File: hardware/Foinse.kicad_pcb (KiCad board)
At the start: 4 copper layers, 60 x 60 mm, 150 parts, among them J1 Conn_02x03_Odd_Even, J10 Conn_02x03_Odd_Even, J2 2060-1452, J3 ESQ-110-14-G-D, J4 PJ-002AH, J5 2060-1452/998-404, J8 2601-1108, J9 USB_C_Receptacle_USB2.0_16P, Q1 AO3400A, Q10 AO3400A, Q11 AO3400A, Q12 AO3400A, Q13 AO3400A, Q14 AO3400A, Q2 AO3400A, Q3 AO3400A, Q4 AO3400A, Q5 AO3400A, Q6 AO3400A, Q7 AO3400A, Q8 AO3400A, Q9 AO3400A, U1 STM32F072C8Tx, U10 LTV-817, U11 LTV-817, U12 LTV-817, U13 LTV-817, U14 USBLC6-2SC6, U15 INA239AIDGSR, U16 INA239AIDGSR, U17 LTC4412xS6, U18 LTV-817, U19 TPS56A37RPAR, U2 TLV70433DBVT, U3 LTV-817, U4 TJA1051T-3, U5 TPS563203, U7 LTV-817, U8 LTV-817, U9 LTV-817

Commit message: folders are indded cool
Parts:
- moved C30 150.3 mm to (135.3, 146.1)
- moved C31 150.3 mm to (107.3, 146.5)
- moved C32 150.3 mm to (132.3, 150.1)
- moved D1 150.3 mm to (120.3, 149.5)
- moved D2 150.3 mm to (132.3, 137.1)
- moved D3 150.3 mm to (104.3, 147.5)
- moved D4 150.3 mm to (107.3, 144.5)
- moved D5 150.3 mm to (96.3, 172.5)
- moved D6 150.3 mm to (107.3, 158.5)
- moved Q1 150.3 mm to (116.3, 143.5)
- moved Q2 150.3 mm to (116.3, 148.5)
- moved Q3 150.3 mm to (121.3, 141.5)
- moved Q4 150.3 mm to (99.3, 156.5)
- moved Q5 150.3 mm to (94.3, 156.5)
- moved Q6 150.3 mm to (111.3, 148.5)
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
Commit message: minor changes
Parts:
- removed C30, C31, C33: 1 uF, Capacitor_SMD:C_0402_1005Metric
- removed D1, D11, D3, D5, D7: RED LED, LED_SMD:LED_0402_1005Metric
- removed D2, D4, D6, D8: GREEN LED, LED_SMD:LED_0402_1005Metric
- removed J1, J10: Conn_02x03_Odd_Even, Connector_PinHeader_1.00mm:PinHeader_2x03_P1.00mm_Vertical
- removed J3: ESQ-110-14-G-D, Foinse Footprints:SAMTEC_ESQ-110-14-G-D
- removed J5: 2060-1452/998-404, Foinse Footprints:WAG
- removed J8: 2601-1108, Foinse Footprints:CONN8_2601-1108_WAG
- removed J9: USB_C_Receptacle_USB2.0_16P, Connector_USB:USB_C_Receptacle_G-Switch_GT-USB-7010ASV
- removed Q1, Q10, Q11, Q12, Q13, Q14, Q2, Q3, Q4, Q5, Q6, Q7, Q8, Q9: AO3400A, Package_TO_SOT_SMD:SOT-23
- removed R10, R30, R39: 2 kΩ, Resistor_SMD:R_0402_1005Metric
- removed R11, R40: 4.7 kΩ, Resistor_SMD:R_0402_1005Metric
- removed R12, R14, R16, R23, R25, R32, R34, R48, R6: 10k Ω, Resistor_SMD:R_0402_1005Metric
- removed R13, R19, R28, R37: 1k Ω, Resistor_SMD:R_0402_1005Metric
- removed R15, R24, R33, R47: 220 Ω, Resistor_SMD:R_0402_1005Metric
- removed R18, R22, R27, R31, R36, R49, R8: 4.7k Ω, Resistor_SMD:R_0402_1005Metric
- removed R20: 6k Ω, Resistor_SMD:R_0402_1005Metric
- removed R21: 2k Ω, Resistor_SMD:R_0402_1005Metric
- removed R29, R38, R9: 6 kΩ, Resistor_SMD:R_0402_1005Metric
- removed R41, R42: 5.1K, Resistor_SMD:R_0402_1005Metric
- removed R43, R44: 10K, Resistor_SMD:R_0402_1005Metric
- removed U10, U11, U12, U13, U18, U3, U7, U8, U9: LTV-817, Foinse Footprints:SO4_TOS
- removed U14: USBLC6-2SC6, Package_TO_SOT_SMD:SOT-23-6
- added J6: JTAG-10 PIN, Connector_IDC:IDC-Header_2x05_P2.54mm_Vertical, F.Cu at (144.9, 106.1)
- C32: value 1 uF -> 100nF
- J2: value 2060-1452 -> XT30PW-M; footprint Foinse Footprints:WAG -> footprints:AMASS_XT30PW-M
- R5: value 220 Ω -> 10kΩ
- moved U4 110.3 mm to (166.3, 89.3)
- moved C2 100.5 mm to (150.4, 81.8)
- moved C1 97.2 mm to (147.2, 85.3), turned to -90 degrees
- moved C6 97.2 mm to (147.2, 88.5), turned to 90 degrees
- moved C7 96.2 mm to (146.2, 88.5), turned to 90 degrees
- moved C5 96.2 mm to (146.2, 85.2), turned to -90 degrees
- moved J2 95.1 mm to (149.8, 53.1)
- moved D9 85.2 mm to (143.5, 67.8), turned to -90 degrees
- moved R5 69.4 mm to (152.7, 81.8)
- moved U1 66.9 mm to (152.8, 87.5)
- moved C10 66.2 mm to (126.2, 126.0)
- moved C11 66.2 mm to (171.2, 112.0)
- moved C12 66.2 mm to (115.2, 105.0)
- moved C13 66.2 mm to (125.2, 134.0)
- moved C14 66.2 mm to (112.2, 104.0)
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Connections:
- C32 pad 1: VBAT_AUX1 -> NRST
- C32 pad 2: /Aux1 neg -> GND
- MOSFET1 pad 2: Net-(J5-1_1) -> Net-(MOSFET1-D)
- R5 pad 1: DROGUE_FIRE -> Net-(U1-BOOT0)
- R5 pad 2: Net-(R5-Pad2) -> GND
- U1 pad 21: DROGUE_SEAT -> unconnected-(U1-PB10-Pad21)
- U1 pad 22: MAIN_SEAT -> unconnected-(U1-PB11-Pad22)
- U1 pad 25: AUX1_SEAT -> unconnected-(U1-PB12-Pad25)
- U1 pad 26: AUX2_SEAT -> unconnected-(U1-PB13-Pad26)
- U1 pad 37: SWCLK -> SWCLK3
- U1 pad 39: DROGUE_FIRE -> unconnected-(U1-PB3-Pad39)
- U1 pad 40: MAIN_FIRE -> unconnected-(U1-PB4-Pad40)
- U1 pad 41: AUX1_FIRE -> unconnected-(U1-PB5-Pad41)
- U1 pad 42: AUX2_FIRE -> unconnected-(U1-PB6-Pad42)
- U1 pad 43: PYRO_ON -> unconnected-(U1-PB7-Pad43)
- U1 pad 44: unconnected-(U1-BOOT0-Pad44) -> Net-(U1-BOOT0)
- U1 pad 45: Mode_sel -> unconnected-(U1-PB8-Pad45)
- U17 pad 1: Net-(J5-1_1) -> Net-(MOSFET1-D)
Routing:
- net Net-(Q12-D): track 14.9 -> 0.00 mm
- net /Aux2 neg: track 4.58 -> 0.00 mm
- net Net-(R37-Pad1): track 2.04 -> 0.00 mm
- net PGND: track 1.94 -> 0.00 mm

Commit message: minor changes
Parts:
- added R4: 10kΩ, Resistor_SMD:R_0402_1005Metric, F.Cu at (146.2, 87.2)
- moved U2 21.8 mm to (190.5, 97.8)
- moved C34 21.8 mm to (187.5, 81.5)
- moved C35 21.8 mm to (187.5, 83.5)
- moved C39 21.8 mm to (190.3, 81.5)
- moved C40 21.8 mm to (190.3, 83.5)
- moved C44 21.8 mm to (193.2, 81.5)
- moved C45 21.8 mm to (193.2, 83.5)
- moved D12 21.8 mm to (180.9, 111.2)
- moved R46 21.8 mm to (186.3, 102.5)
- moved R51 21.8 mm to (189.3, 102.5)
- moved R53 21.8 mm to (189.3, 106.5)
- moved R54 21.8 mm to (189.3, 108.5)
- moved R56 21.8 mm to (192.2, 102.5)
- moved R58 21.8 mm to (192.2, 106.5)
- moved U17 21.8 mm to (176.7, 110.6)
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
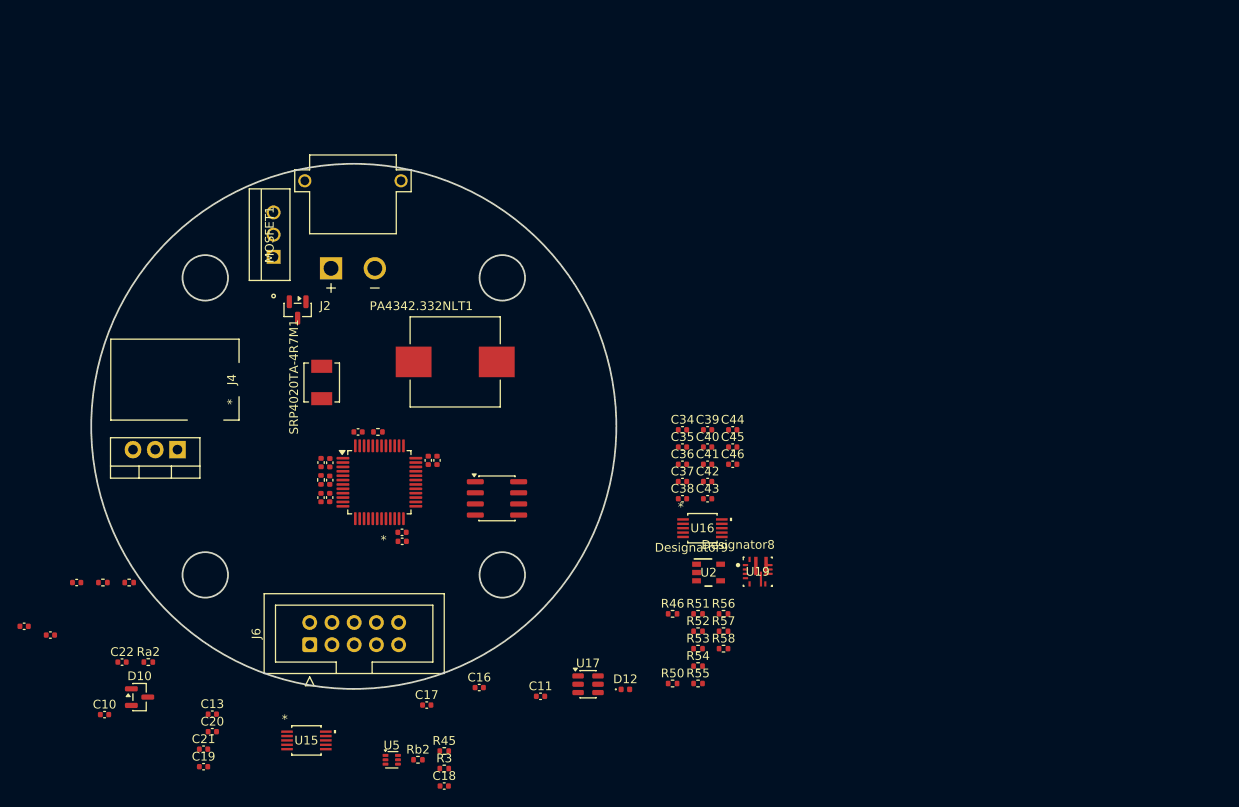
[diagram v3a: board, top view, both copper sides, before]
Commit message: 5v logic routed
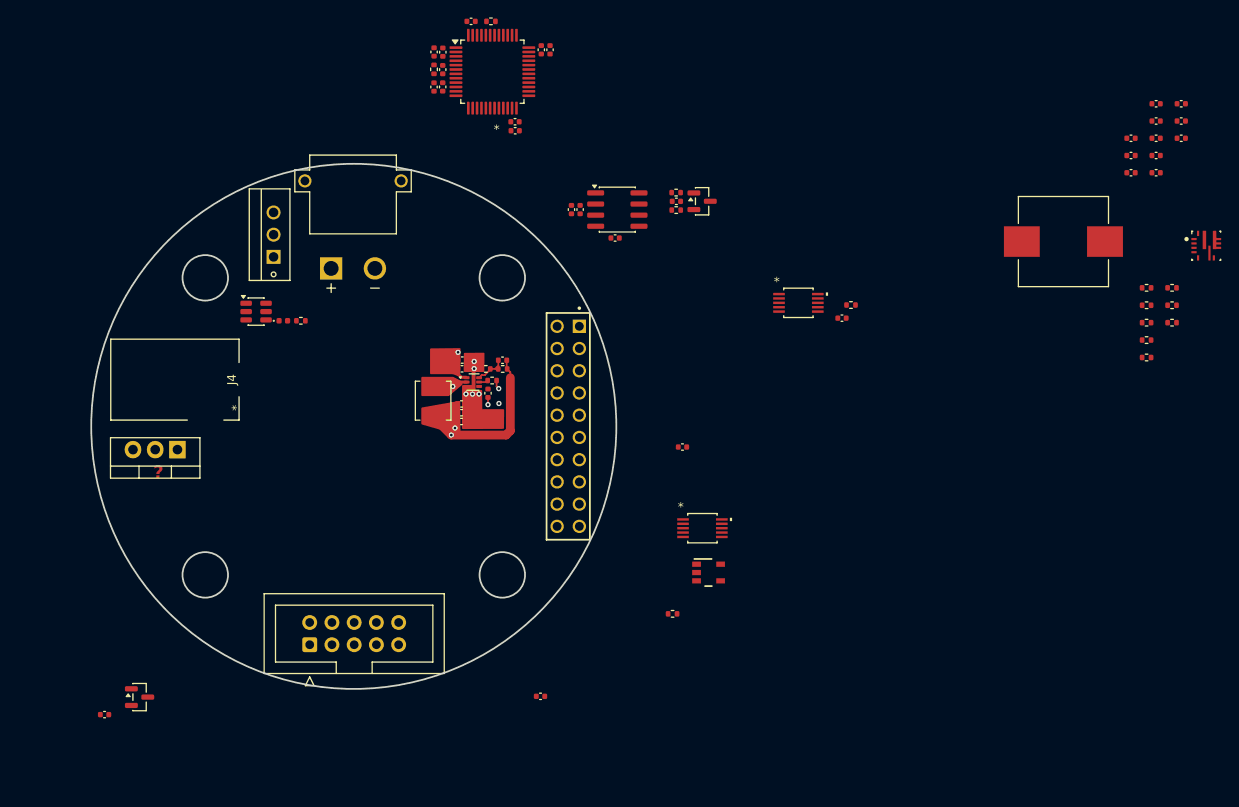
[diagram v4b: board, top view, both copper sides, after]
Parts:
- added J1: ESQ-110-X-X-D, footprints:SAMTEC_ESQ-110-14-G-D, F.Cu at (174.4, 81.1)
- Ra2: value 220 Ω -> 220Ω
- Rb2: value 30 Ω -> 30Ω
- moved C15 81.2 mm to (186.8, 55.4)
- moved C14 80.8 mm to (179.8, 59.6), turned to 180 degrees
- moved R2 79.2 mm to (186.7, 54.4), turned to 180 degrees
- moved C12 76.9 mm to (174.8, 56.3), turned to 90 degrees
- moved R1 75.6 mm to (186.8, 56.4)
- moved U15 75.2 mm to (200.7, 67.0)
- moved C13 71.3 mm to (175.8, 56.3), turned to 90 degrees
- moved PA4342.332NLT1 70.8 mm to (231.0, 60.0)
- moved R45 69.0 mm to (206.7, 67.3)
- moved C36 63.4 mm to (238.7, 48.2)
- moved C37 63.4 mm to (238.7, 50.2)
- moved C38 63.4 mm to (238.7, 52.1)
- moved C41 63.4 mm to (241.6, 48.2)
- moved C42 63.4 mm to (241.6, 50.2)
- moved C43 63.4 mm to (241.6, 52.1)
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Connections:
- SRP4020TA-4R7M1 pad 1: unconnected-(SRP4020TA-4R7M1-Pad1) -> Net-(U5-SW)
- SRP4020TA-4R7M1 pad 2: unconnected-(SRP4020TA-4R7M1-Pad2) -> 5VLOGIC
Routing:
- net 5VLOGIC: track 0.00 -> 18.1 mm, vias 0 -> 2
- net VBAT: track 0.00 -> 12.8 mm, vias 0 -> 2
- net Net-(U5-SW): track 0.00 -> 9.94 mm, vias 0 -> 2
- net Net-(U5-FB): track 0.00 -> 3.65 mm
- net Net-(U5-EN): track 0.00 -> 1.06 mm
- net GND: vias 0 -> 6
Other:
- board text added: "?"

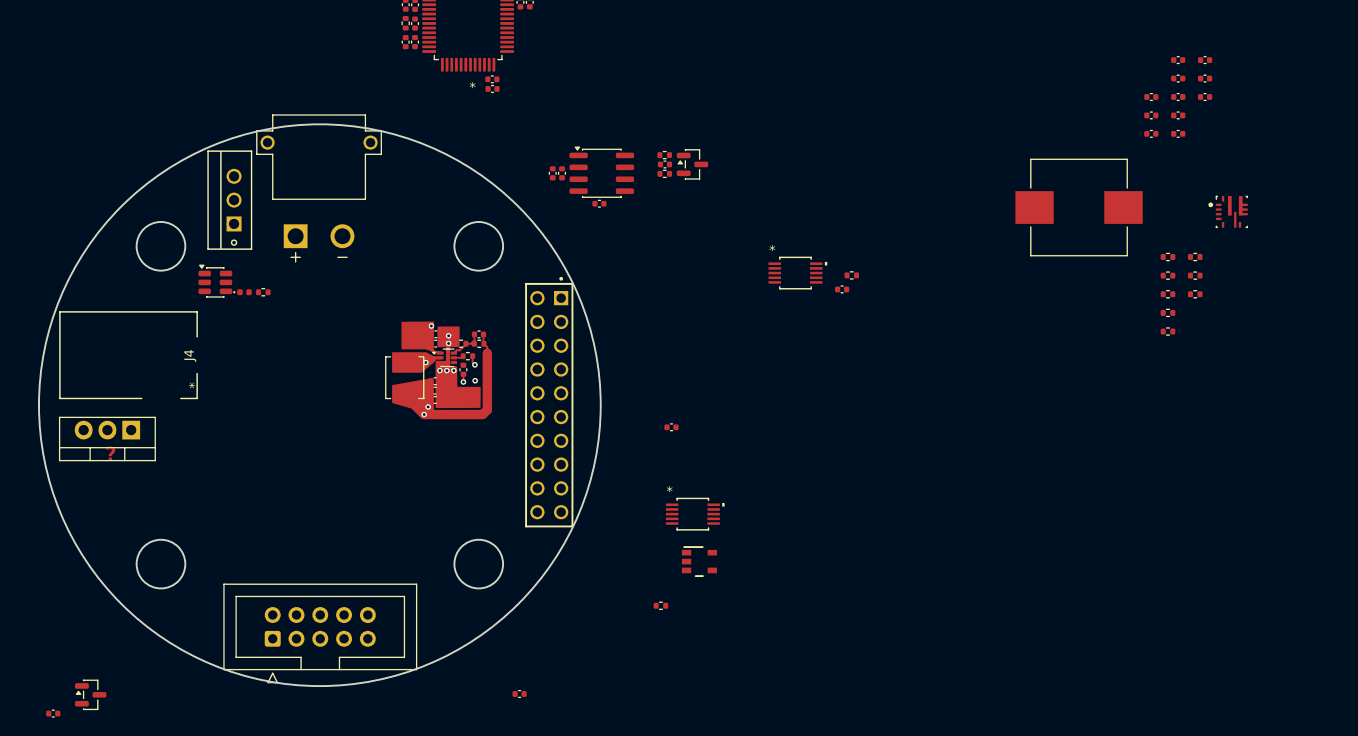
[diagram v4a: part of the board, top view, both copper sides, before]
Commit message: new inductor
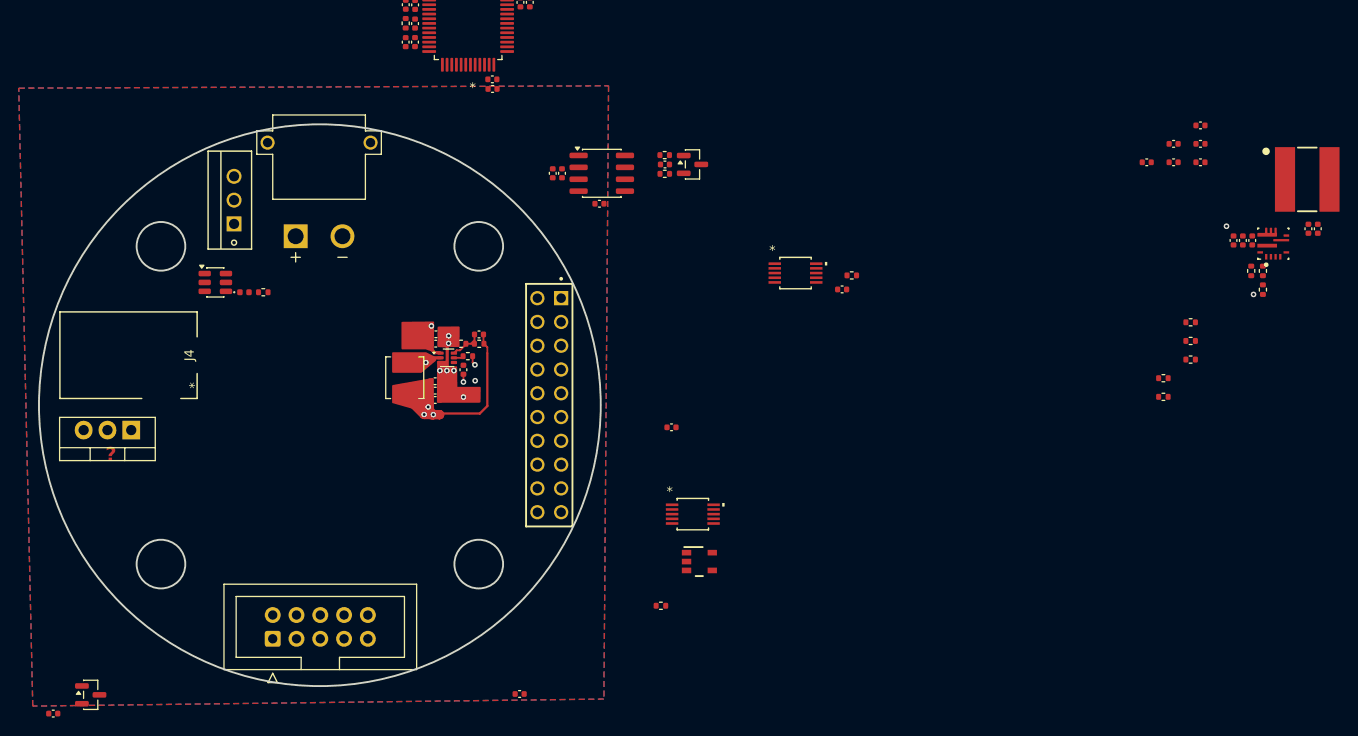
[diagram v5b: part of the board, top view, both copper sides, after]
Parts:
- removed PA4342.332NLT1: 3.3 uH, Foinse Footprints:IND_PA4342.332NLT
- added L1: WE-MAPI_6030, footprints:WE-MAPI_6030, F.Cu at (255.4, 57.0)
- R54, R57: value DNP -> 0
- moved C39 20.5 mm to (248.5, 63.5), turned to -90 degrees
- moved C42 18.4 mm to (255.5, 62.3), turned to 90 degrees
- moved C43 18.0 mm to (256.5, 62.3), turned to 90 degrees
- moved C37 17.2 mm to (249.5, 63.5), turned to -90 degrees
- moved C38 14.4 mm to (247.5, 63.5), turned to -90 degrees
- moved R53 10.4 mm to (250.6, 66.8), turned to -90 degrees
- moved R52 10.2 mm to (250.6, 68.8), turned to 90 degrees
- moved R51 9.01 mm to (249.4, 66.8), turned to -90 degrees
- moved R54 6.99 mm to (240.0, 78.2)
- moved R56 6.99 mm to (242.9, 72.3)
- moved C36 6.99 mm to (238.2, 55.2)
- moved C40 6.99 mm to (241.1, 53.2)
- moved C41 6.99 mm to (241.1, 55.2)
- moved C45 6.99 mm to (244.0, 53.2)
- moved C46 6.99 mm to (244.0, 55.2)
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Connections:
- C42 pad 2: PGND2 -> GND
- C43 pad 2: PGND2 -> GND
- C44 pad 2: PGND2 -> GND
- C45 pad 2: PGND2 -> GND
- C46 pad 2: PGND2 -> GND
- U19 pad 9: PGND2 -> GND
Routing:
- net 5VLOGIC: track 18.1 -> 23.8 mm, vias 2 -> 3
- net VBAT: vias 2 -> 4
- net GND: vias 6 -> 7
- added copper zone on B.Cu, net GND
- added copper zone on F.Cu, net GND
- added copper zone on In1.Cu, net GND
- added copper zone on In2.Cu, net GND

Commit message: new inductor2
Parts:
- moved C44 26.9 mm to (255.8, 75.3)
- moved C36 26.9 mm to (250.1, 79.3)
- moved C40 26.9 mm to (252.9, 77.3)
- moved C41 26.9 mm to (252.9, 79.3)
- moved C45 26.9 mm to (255.8, 77.3)
- moved C46 26.9 mm to (255.8, 79.3)
- moved R56 23.4 mm to (264.5, 63.2)
- moved R57 23.4 mm to (264.5, 65.2)
- moved R58 23.4 mm to (264.5, 67.2)
- moved R54 19.1 mm to (258.0, 71.8)
- moved R55 19.1 mm to (258.0, 73.7)
- moved L1 0.62 mm to (254.8, 57.0)
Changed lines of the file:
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@@
 	(footprint "Capacitor_SMD:C_0402_1005Metric"
 		(layer "F.Cu")
-		(at 243.97 51.23)
+		(at 255.81 75.34)
 		(descr "Capacitor SMD 0402 (1005 Metric), square (rectangular) end terminal, IPC-7351 nominal, (Body size source: IPC-SM-782 page 76, https://www.pcb-3d.com/wordpress/wp-content/uploads/ipc-sm-782a_amendment_1_and_2.pdf), generated with kicad-footprint-generator")
 		(tags "capacitor")
@@
 	(footprint "Resistor_SMD:R_0402_1005Metric"
 		(layer "F.Cu")
-		(at 242.92 72.26)
+		(at 264.5 63.25)
 		(descr "Resistor SMD 0402 (1005 Metric), square (rectangular) end terminal, IPC-7351 nominal, (Body size source: IPC-SM-782 page 72, https://www.pcb-3d.com/wordpress/wp-content/uploads/ipc-sm-782a_amendment_1_and_2.pdf), generated with kicad-footprint-generator")
 		(tags "resistor")
@@
 	(footprint "footprints:WE-MAPI_6030"
 		(layer "F.Cu")
-		(at 255.375 57)
+		(at 254.75 57)
 		(property "Reference" "L1"
 			(at 0 -4.635 0)
@@
 			(polygon
 				(pts
-					(xy 254.075 53.55) (xy 256.675 53.55) (xy 256.675 60.45) (xy 254.075 60.45)
+					(xy 253.45 53.55) (xy 256.05 53.55) (xy 256.05 60.45) (xy 253.45 60.45)
 				)
 			)
@@
 			(polygon
 				(pts
-					(xy 254.075 53.55) (xy 256.675 53.55) (xy 256.675 60.45) (xy 254.075 60.45)
+					(xy 253.45 53.55) (xy 256.05 53.55) (xy 256.05 60.45) (xy 253.45 60.45)
 				)
 			)
 		)
 		(embedded_fonts no)
+		(model "${KIPRJMOD}/Lib/footprints.pretty/STP_74438377.STEP"
+			(offset
+				(xyz 0 0 0)
+			)
+			(scale
+				(xyz 1 1 1)
+			)
+			(rotate
+				(xyz -0 -0 -0)
+			)
+		)
 	)
 	(footprint "Capacitor_SMD:C_0402_1005Metric"
@@
 	(footprint "Capacitor_SMD:C_0402_1005Metric"
 		(layer "F.Cu")
-		(at 241.1 53.2)
+		(at 252.94 77.31)
 		(descr "Capacitor SMD 0402 (1005 Metric), square (rectangular) end terminal, IPC-7351 nominal, (Body size source: IPC-SM-782 page 76, https://www.pcb-3d.com/wordpress/wp-content/uploads/ipc-sm-782a_amendment_1_and_2.pdf), generated with kicad-footprint-generator")
 		(tags "capacitor")
@@
 	(footprint "Capacitor_SMD:C_0402_1005Metric"
 		(layer "F.Cu")
-		(at 241.1 55.17)
+		(at 252.94 79.28)
 		(descr "Capacitor SMD 0402 (1005 Metric), square (rectangular) end terminal, IPC-7351 nominal, (Body size source: IPC-SM-782 page 76, https://www.pcb-3d.com/wordpress/wp-content/uploads/ipc-sm-782a_amendment_1_and_2.pdf), generated with kicad-footprint-generator")
 		(tags "capacitor")
@@
 	(footprint "Capacitor_SMD:C_0402_1005Metric"
 		(layer "F.Cu")
-		(at 243.97 55.17)
+		(at 255.81 79.28)
 		(descr "Capacitor SMD 0402 (1005 Metric), square (rectangular) end terminal, IPC-7351 nominal, (Body size source: IPC-SM-782 page 76, https://www.pcb-3d.com/wordpress/wp-content/uploads/ipc-sm-782a_amendment_1_and_2.pdf), generated with kicad-footprint-generator")
 		(tags "capacitor")
@@
 	(footprint "Resistor_SMD:R_0402_1005Metric"
 		(layer "F.Cu")
-		(at 242.92 76.24)
+		(at 264.5 67.23)
 		(descr "Resistor SMD 0402 (1005 Metric), square (rectangular) end terminal, IPC-7351 nominal, (Body size source: IPC-SM-782 page 72, https://www.pcb-3d.com/wordpress/wp-content/uploads/ipc-sm-782a_amendment_1_and_2.pdf), generated with kicad-footprint-generator")
 		(tags "resistor")
@@
 	(footprint "Resistor_SMD:R_0402_1005Metric"
 		(layer "F.Cu")
-		(at 240.01 78.23)
+		(at 258.01 71.75)
 		(descr "Resistor SMD 0402 (1005 Metric), square (rectangular) end terminal, IPC-7351 nominal, (Body size source: IPC-SM-782 page 72, https://www.pcb-3d.com/wordpress/wp-content/uploads/ipc-sm-782a_amendment_1_and_2.pdf), generated with kicad-footprint-generator")
 		(tags "resistor")
@@
 	(footprint "Capacitor_SMD:C_0402_1005Metric"
 		(layer "F.Cu")
-		(at 243.97 53.2)
+		(at 255.81 77.31)
 		(descr "Capacitor SMD 0402 (1005 Metric), square (rectangular) end terminal, IPC-7351 nominal, (Body size source: IPC-SM-782 page 76, https://www.pcb-3d.com/wordpress/wp-content/uploads/ipc-sm-782a_amendment_1_and_2.pdf), generated with kicad-footprint-generator")
 		(tags "capacitor")
@@
 	(footprint "Capacitor_SMD:C_0402_1005Metric"
 		(layer "F.Cu")
-		(at 238.23 55.17)
+		(at 250.07 79.28)
 		(descr "Capacitor SMD 0402 (1005 Metric), square (rectangular) end terminal, IPC-7351 nominal, (Body size source: IPC-SM-782 page 76, https://www.pcb-3d.com/wordpress/wp-content/uploads/ipc-sm-782a_amendment_1_and_2.pdf), generated with kicad-footprint-generator")
 		(tags "capacitor")
@@
 	(footprint "Resistor_SMD:R_0402_1005Metric"
 		(layer "F.Cu")
-		(at 242.92 74.25)
+		(at 264.5 65.24)
 		(descr "Resistor SMD 0402 (1005 Metric), square (rectangular) end terminal, IPC-7351 nominal, (Body size source: IPC-SM-782 page 72, https://www.pcb-3d.com/wordpress/wp-content/uploads/ipc-sm-782a_amendment_1_and_2.pdf), generated with kicad-footprint-generator")
 		(tags "resistor")
@@
 	(footprint "Resistor_SMD:R_0402_1005Metric"
 		(layer "F.Cu")
-		(at 240.01 80.22)
+		(at 258.01 73.74)
 		(descr "Resistor SMD 0402 (1005 Metric), square (rectangular) end terminal, IPC-7351 nominal, (Body size source: IPC-SM-782 page 72, https://www.pcb-3d.com/wordpress/wp-content/uploads/ipc-sm-782a_amendment_1_and_2.pdf), generated with kicad-footprint-generator")
 		(tags "resistor")
